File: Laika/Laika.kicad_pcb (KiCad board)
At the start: 2 copper layers, 17 parts, among them J1 61083-041402LF, J2 Micro_SD_Card, J3 61082-041602LF, U1 LSM6DSL, U2 MS5611-01BA, U3 RASPBERRY_PI_ZERO_2_W, U4 MMC5983MA

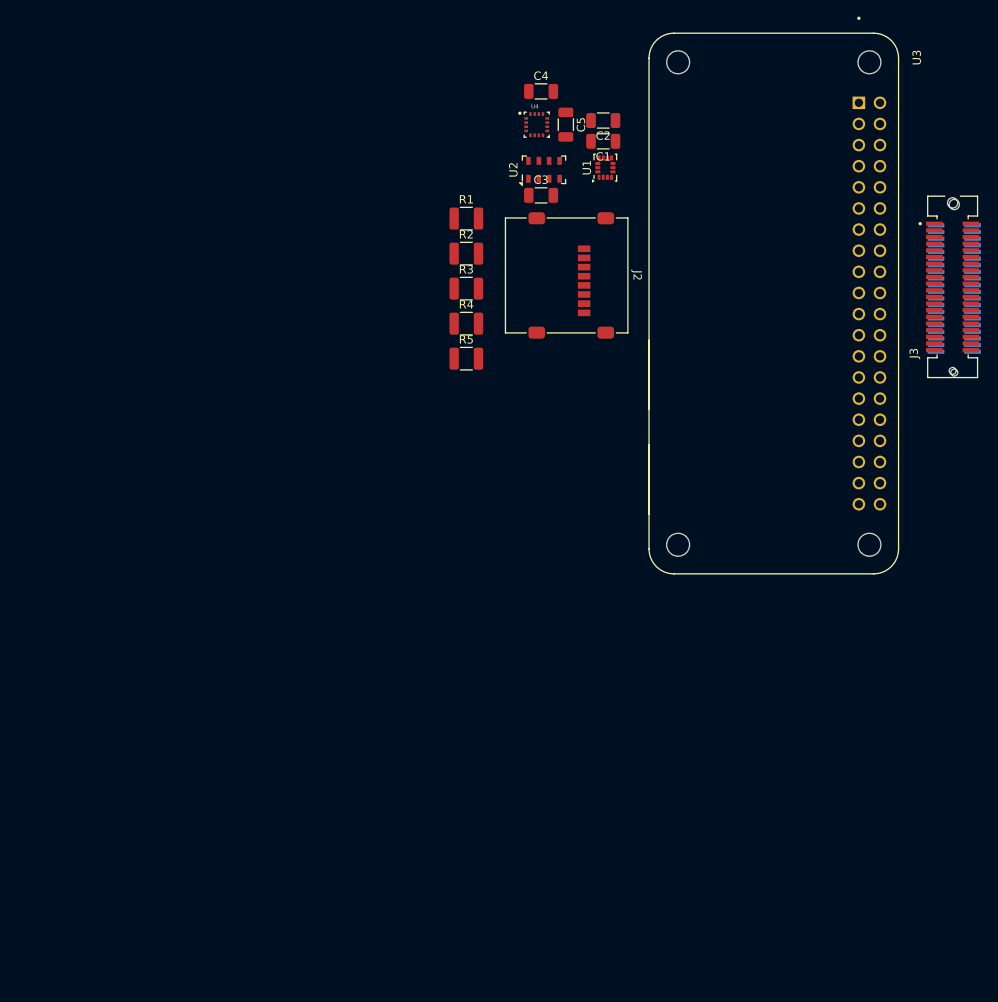
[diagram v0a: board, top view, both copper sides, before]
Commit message: RS485 hookup, new accelerometer, connectors, edgecuts
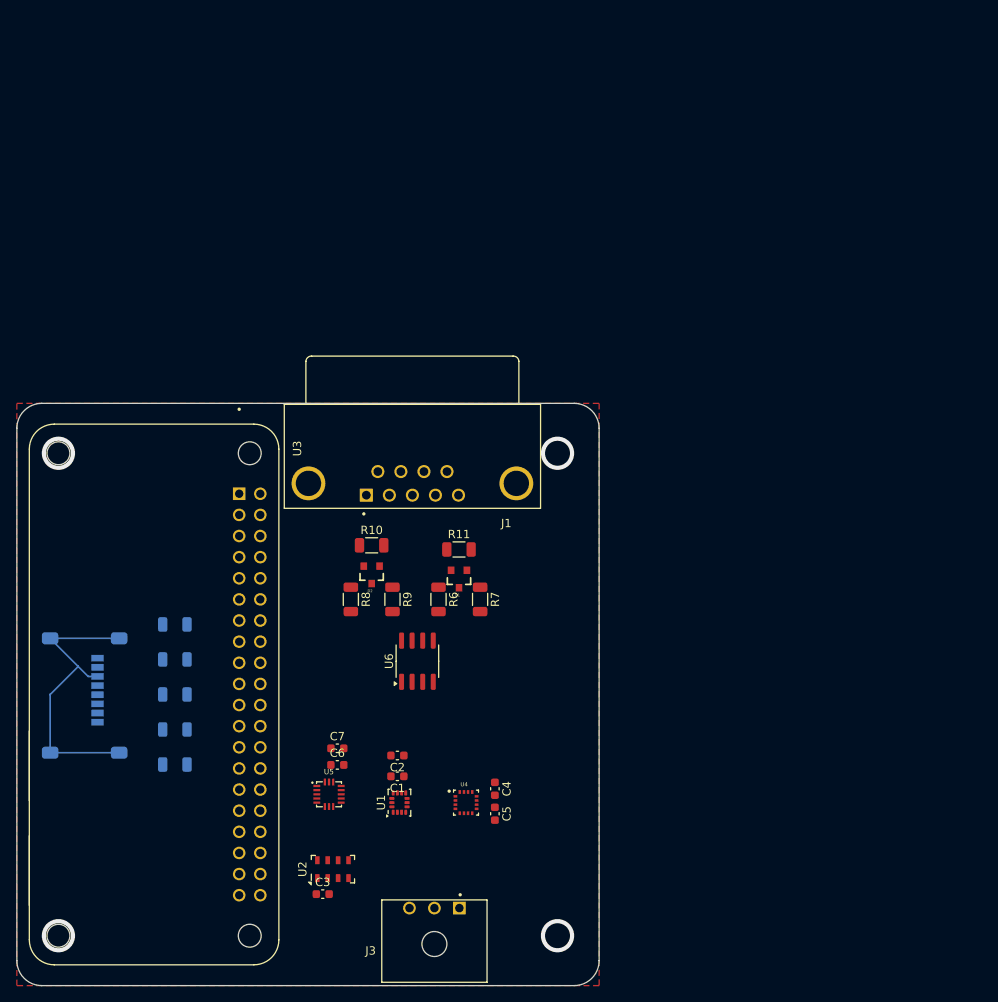
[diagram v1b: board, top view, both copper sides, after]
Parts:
- added C6: 100n, Capacitor_SMD:C_0603_1608Metric, F.Cu at (88.5, 123.5)
- added C7: 10u, Capacitor_SMD:C_0603_1608Metric, F.Cu at (88.5, 121.5)
- added D1: CDSOT23-SM712, CDSOT23-SM712:SOT23-3, F.Cu at (103.2, 101.1)
- added D2: CDSOT23-SM712, CDSOT23-SM712:SOT23-3, F.Cu at (92.7, 100.6)
- added R10: R, Resistor_SMD:R_1206_3216Metric, F.Cu at (92.7, 97.1)
- added R11: R, Resistor_SMD:R_1206_3216Metric, F.Cu at (103.2, 97.6)
- added R6: 10, Resistor_SMD:R_1206_3216Metric, F.Cu at (100.7, 103.6)
- added R7: 10, Resistor_SMD:R_1206_3216Metric, F.Cu at (105.7, 103.6)
- added R8: 10, Resistor_SMD:R_1206_3216Metric, F.Cu at (90.2, 103.6)
- added R9: 10, Resistor_SMD:R_1206_3216Metric, F.Cu at (95.2, 103.6)
- added U5: H3LIS331DLTR, H3LIS331DLTR:QFN300X300X100-16N, F.Cu at (87.5, 127.0)
- added U6: THVD1451D, Package_SO:SOIC-8_3.9x4.9mm_P1.27mm, F.Cu at (98.2, 111.0)
- C1, C2, C3, C4, C5: footprint Capacitor_SMD:C_1206_3216Metric -> Capacitor_SMD:C_0603_1608Metric
- J1: value 61083-041402LF -> A-DF_09_A_KG-T4S; footprint 61083-041402LF:AMPHENOL_61083-041402LF -> A-DF 09 AKG-T4S:ASSMANN_A-DF_09_A_KG-T4S; moved to F.Cu
- J2: moved to B.Cu
- J3: value 61082-041602LF -> 0436500300; footprint 61082-041602LF:AMPHENOL_61082-041602LF -> 0436500300:MOLEX_0436500300
- R1, R2, R3, R4, R5: footprint Resistor_SMD:R_1210_3225Metric -> Resistor_SMD:R_1206_3216Metric; moved to B.Cu
- moved J3 97.3 mm to (100.2, 140.7), turned to 0 degrees
- moved U3 88.1 mm to (66.5, 115.0)
- moved C3 88.0 mm to (86.8, 139.0)
- moved U2 87.8 mm to (88.0, 136.0)
- moved C4 84.0 mm to (107.5, 126.3), turned to -90 degrees
- moved C5 83.3 mm to (107.5, 129.3)
- moved U4 81.9 mm to (104.0, 128.0)
- moved C1 80.2 mm to (95.8, 124.8)
- moved C2 80.2 mm to (95.8, 122.3)
- moved U1 80.2 mm to (96.0, 128.0)
- moved J2 77.3 mm to (57.6, 115.1), turned to 90 degrees
- moved J1 74.9 mm to (92.0, 91.0), turned to 180 degrees
- moved R1 60.1 mm to (69.0, 106.6), turned to 180 degrees
- moved R2 60.1 mm to (69.0, 110.8), turned to 180 degrees
- moved R3 60.1 mm to (69.0, 115.0), turned to 180 degrees
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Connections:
- J1 pad 2: unconnected-(J1-Pad2) -> MODBUS_RX_P
- J1 pad 3: unconnected-(J1-Pad3) -> MODBUS_TX_P
- J1 pad 5: unconnected-(J1-Pad5) -> GND
- J1 pad 8: unconnected-(J1-Pad8) -> MODBUS_RX_N
- J1 pad 9: unconnected-(J1-Pad9) -> MODBUS_TX_N
- J3 pad 1: unconnected-(J3-Pad1) -> +5V
- J3 pad 2: unconnected-(J3-Pad2) -> GND
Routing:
- net GND: track 0.00 -> 36.0 mm
- net (no net): vias 0 -> 4
- added copper zone on F.Cu, net GND
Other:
- board outline added: 70 x 70 mm

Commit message: Version 0A
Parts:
- removed D1, D2: CDSOT23-SM712, CDSOT23-SM712:SOT23-3
- removed R10, R11: R, Resistor_SMD:R_1206_3216Metric
- removed R6, R7, R8, R9: 10, Resistor_SMD:R_1206_3216Metric
- added J4: DF52-8S-0.8H_21_, Hirose D52:HIROSE_DF52-8S-0.8H_21_, B.Cu at (128.5, 69.9)
- C1, C2, C3, C4, C5, C6, C7, U1, U2, U4, U5: moved to B.Cu
- J1: value A-DF_09_A_KG-T4S -> DF52-8S-0.8H_21_; footprint A-DF 09 AKG-T4S:ASSMANN_A-DF_09_A_KG-T4S -> Hirose D52:HIROSE_DF52-8S-0.8H_21_; moved to B.Cu
- U6: value THVD1451D -> PCA9685PW; footprint Package_SO:SOIC-8_3.9x4.9mm_P1.27mm -> Package_SO:TSSOP-28_4.4x9.7mm_P0.65mm; moved to B.Cu
- moved U3 79.1 mm to (140.1, 86.0)
- moved J2 76.3 mm to (130.6, 92.8)
- moved R2 76.3 mm to (141.6, 87.2), turned to -90 degrees
- moved R4 75.5 mm to (141.6, 98.4), turned to 90 degrees
- moved R3 74.8 mm to (140.6, 93.1), turned to 0 degrees
- moved R5 74.6 mm to (139.3, 98.4), turned to 90 degrees
- moved R1 72.9 mm to (139.3, 87.2), turned to -90 degrees
- moved C3 62.6 mm to (145.6, 117.4), turned to 180 degrees
- moved U2 60.4 mm to (144.6, 114.7)
- moved U6 54.7 mm to (138.6, 74.2)
- moved U5 49.9 mm to (135.8, 114.5)
- moved C6 44.5 mm to (132.1, 114.5), turned to 180 degrees
- moved U1 44.1 mm to (132.7, 103.5)
- moved J3 43.9 mm to (140.1, 122.2)
- moved C7 43.9 mm to (132.1, 116.0), turned to 180 degrees
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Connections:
- J1 pad 1: unconnected-(J1-Pad1) -> PWM_0
- J1 pad 2: MODBUS_RX_P -> PWM_1
- J1 pad 3: MODBUS_TX_P -> PWM_2
- J1 pad 4: unconnected-(J1-Pad4) -> PWM_3
- J1 pad 5: GND -> PWM_4
- J1 pad 6: unconnected-(J1-Pad6) -> PWM_5
- J1 pad 7: unconnected-(J1-Pad7) -> PWM_6
- J1 pad 8: MODBUS_RX_N -> PWM_7
- U6 pad 1: +3.3V -> GND
- U6 pad 2: PI_UART_RX -> GND
- U6 pad 3: PI_UART_TX -> GND
- U6 pad 5: Net-(U6-Y) -> GND
- U6 pad 6: Net-(U6-Z) -> PWM_0
- U6 pad 7: Net-(U6-B) -> PWM_1
- U6 pad 8: Net-(U6-A) -> PWM_2
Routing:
- net +5V: track 0.00 -> 84.9 mm
- net GND: track 36.0 -> 94.2 mm, vias 0 -> 12
- net BUS_SPI1_CE1: track 0.00 -> 51.3 mm
- net BUS_SPI1_SCLK: track 0.00 -> 47.7 mm, vias 0 -> 2
- net BUS_SPI1_MOSI: track 0.00 -> 46.0 mm, vias 0 -> 2
- net PI_GPIO_27: track 0.00 -> 45.3 mm, vias 0 -> 1
- net BUS_SPI1_CE0: track 0.00 -> 44.2 mm
- net +3.3V: track 0.00 -> 42.5 mm, vias 0 -> 10
- net BUS_SPI1_MISO: track 0.00 -> 39.3 mm
- net BUS_SPI0_MOSI: track 0.00 -> 28.8 mm
- net BUS_SPI0_CE0: track 0.00 -> 28.6 mm
- net BUS_SPI0_MISO: track 0.00 -> 27.4 mm
- net BUS_SPI0_SCLK: track 0.00 -> 26.2 mm
- net BUS_SPI1_CE2: track 0.00 -> 24.3 mm
- net PWM_0: track 0.00 -> 14.0 mm
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- added copper zone on F.Cu, net +3.3V
- added copper zone on B.Cu, net GND
- removed copper zone on F.Cu, net GND
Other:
- board size 70 x 70 mm -> 30.2 x 77.8 mm
- board text added: "Laika Flight Computer"
- board text added: "Made on Earth by Humans"
- board text added: "Rev 0A"
